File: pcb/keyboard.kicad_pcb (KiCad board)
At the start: 2 copper layers, 219 x 100.2 mm, 50 parts, among them J1 TRRS, SW11 11, SW12 12, SW13 13, SW14 14, SW15 15, SW16 16, SW17 17, SW18 18, SW19 19, SW21 21, SW22 22, SW23 23, SW24 24, SW25 25, SW26 26, SW27 27, SW28 28, SW29 29, SW31 31, SW32 32, SW33 33, SW34 34, SW35 35, SW36 36, SW37 37, SW38 38, SW39 39, SW41 41, SW42 42, SW43 43, SW45 45, SW46 46, SW47 47, SW48 48, SW49 49, U1 EliteC

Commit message: add traces to numpad
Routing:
- net (no net): track 385.5 -> 0.00 mm
- net COL9: track 0.00 -> 271.6 mm, vias 0 -> 4
- net COL8: track 0.00 -> 252.2 mm, vias 0 -> 4
- net COL7: track 0.00 -> 226.7 mm, vias 0 -> 4
- net ROW2: track 155.9 -> 276.8 mm
- net ROW4: track 40.3 -> 149.6 mm
- net ROW1: track 141.0 -> 235.3 mm
- net ROW3: track 174.9 -> 265.5 mm
- net Net-(SW27-Pad3): track 0.00 -> 33.5 mm
- net Net-(SW38-Pad3): track 0.00 -> 33.5 mm
- net Net-(SW48-Pad3): track 0.00 -> 33.5 mm
- net Net-(SW19-Pad3): track 0.00 -> 33.5 mm
- net Net-(SW49-Pad3): track 0.00 -> 33.5 mm
- net Net-(SW47-Pad3): track 0.00 -> 33.5 mm
- net Net-(SW29-Pad3): track 0.00 -> 33.5 mm
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
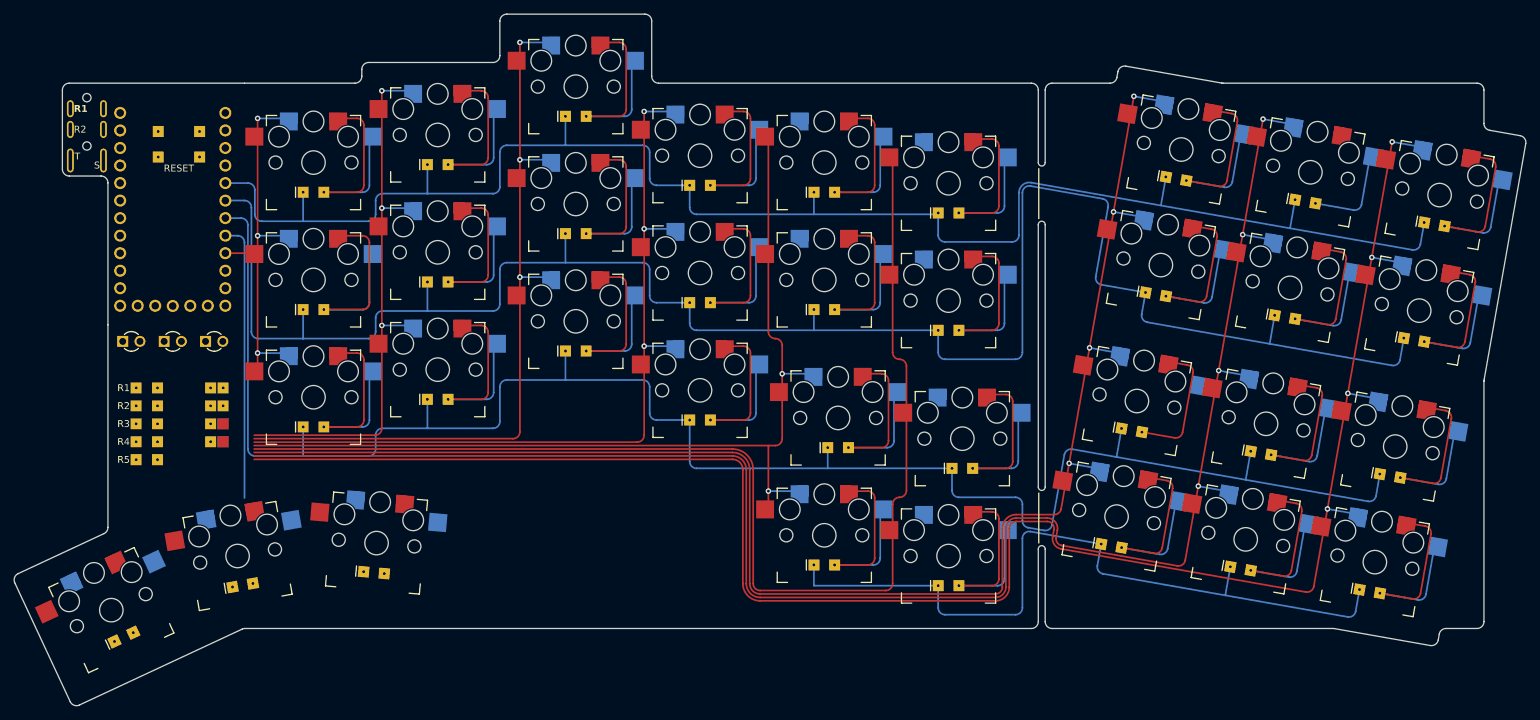
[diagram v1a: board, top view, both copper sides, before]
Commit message: use polygon instead of drill offset for switch footprint
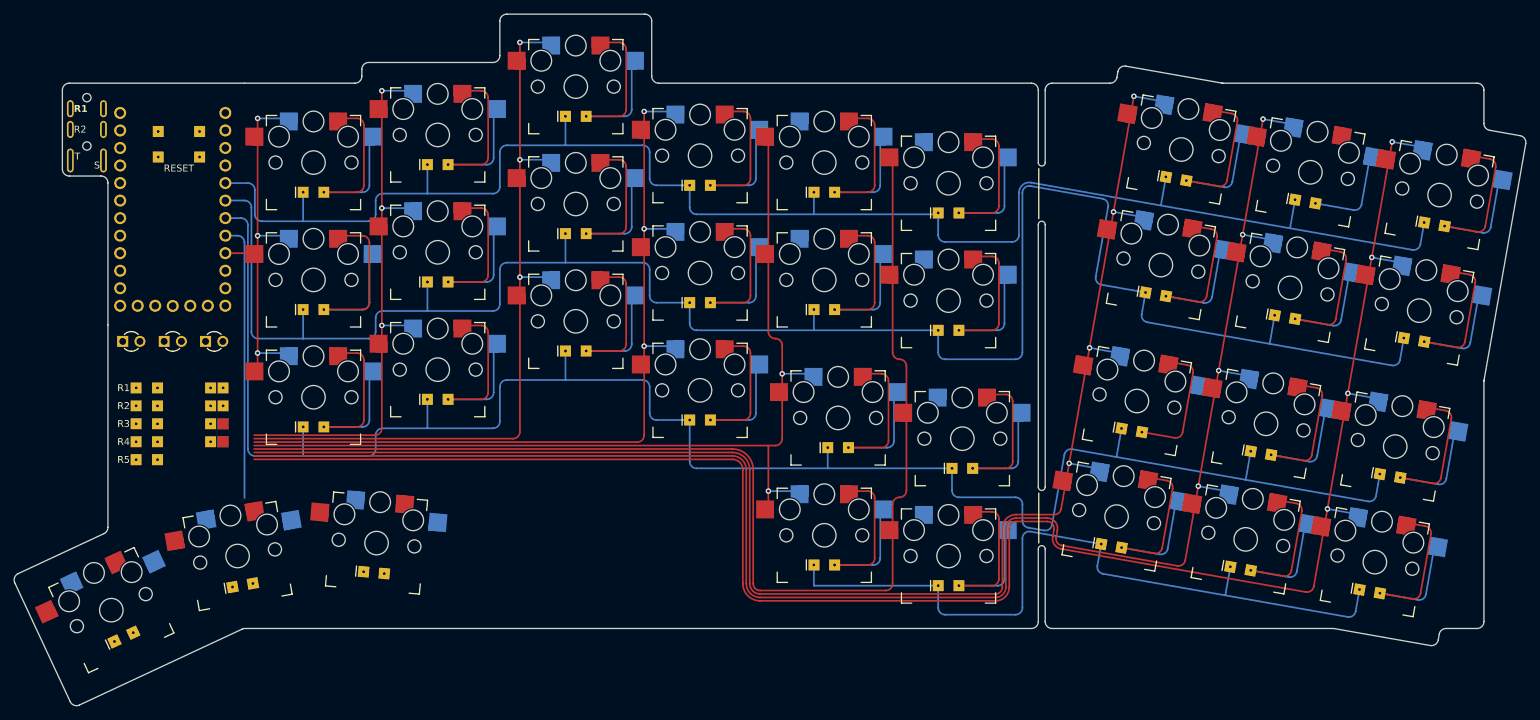
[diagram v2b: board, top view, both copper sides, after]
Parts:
- JP1, JP2: value Jumper -> JumperSplit

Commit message: correct traces with new layout
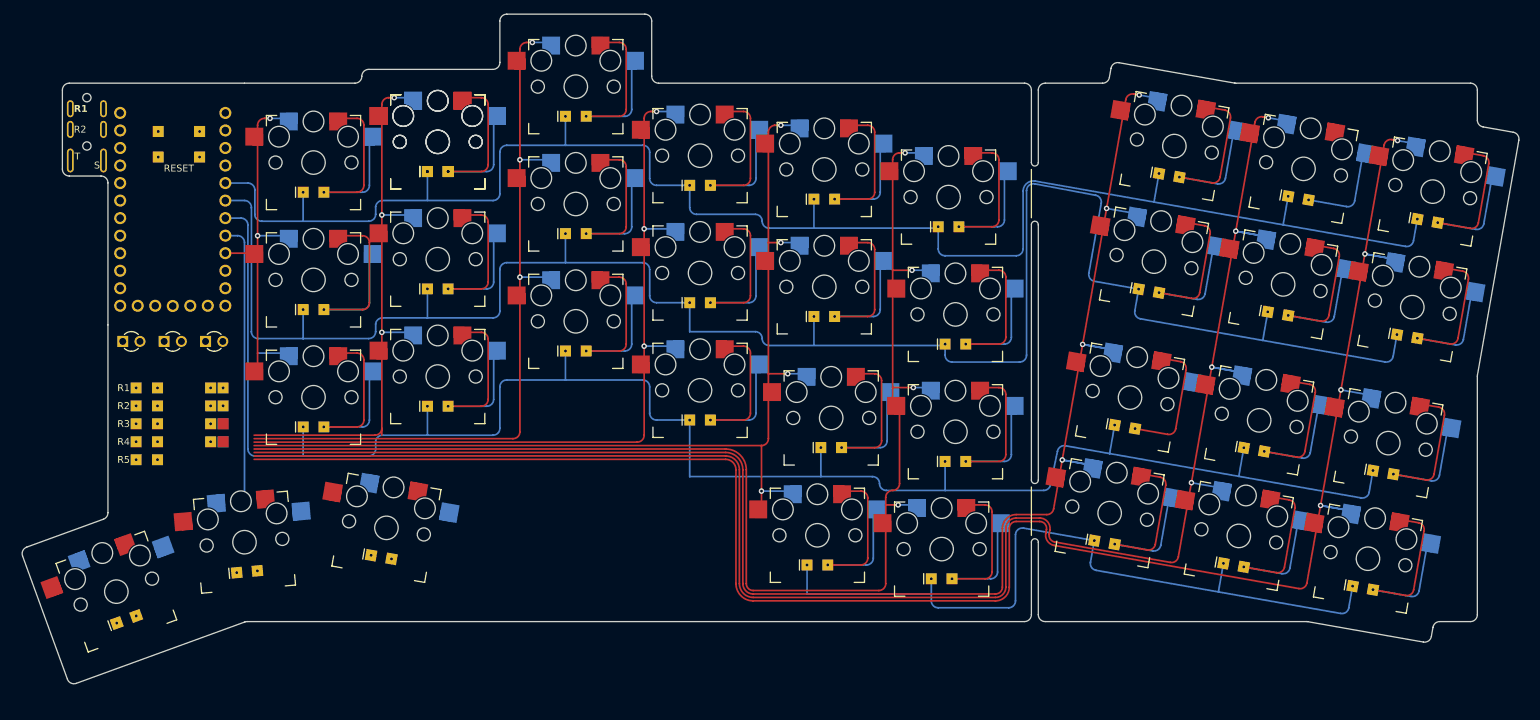
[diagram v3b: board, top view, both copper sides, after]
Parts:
- added SW12: 12, Keyboard:Switch, F.Cu at (99.5, 58.0)
- moved SW41 2.78 mm to (52.9, 123.2), turned to 20 degrees
- moved SW43 2.63 mm to (92.1, 113.9), turned to -10 degrees
- moved SW26 2.24 mm to (174.5, 83.0)
- moved SW42 2.24 mm to (71.5, 116.0), turned to 5 degrees
- moved SW16 2.00 mm to (173.5, 66.0)
- moved SW36 1.41 mm to (174.5, 100.0)
- moved SW46 1.41 mm to (172.5, 117.0)
- moved SW17 1.12 mm to (206.2, 58.6)
- moved SW18 1.12 mm to (224.9, 61.9)
- moved SW19 1.12 mm to (243.6, 65.2)
- moved SW27 1.12 mm to (203.3, 75.4)
- moved SW28 1.12 mm to (222.0, 78.7)
- moved SW29 1.12 mm to (240.7, 82.0)
- moved SW37 1.12 mm to (199.8, 95.0)
- moved SW38 1.12 mm to (218.5, 98.3)
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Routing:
- net COL6: track 175.1 -> 196.6 mm, vias 0 -> 4
- net COL5: track 141.1 -> 151.7 mm, vias 2 -> 4
- net COL7: track 226.7 -> 235.7 mm
- net COL8: track 252.2 -> 260.1 mm
- net COL9: track 271.6 -> 279.5 mm
- net ROW3: track 265.5 -> 260.8 mm
- net ROW1: track 235.3 -> 238.6 mm
- net ROW2: track 276.8 -> 278.0 mm
- net ROW4: track 149.6 -> 150.3 mm
- net COL1: track 56.8 -> 56.3 mm, vias 3 -> 2
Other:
- board size 219 x 100.2 mm -> 216.8 x 97 mm

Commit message: add traces for thumb cluster
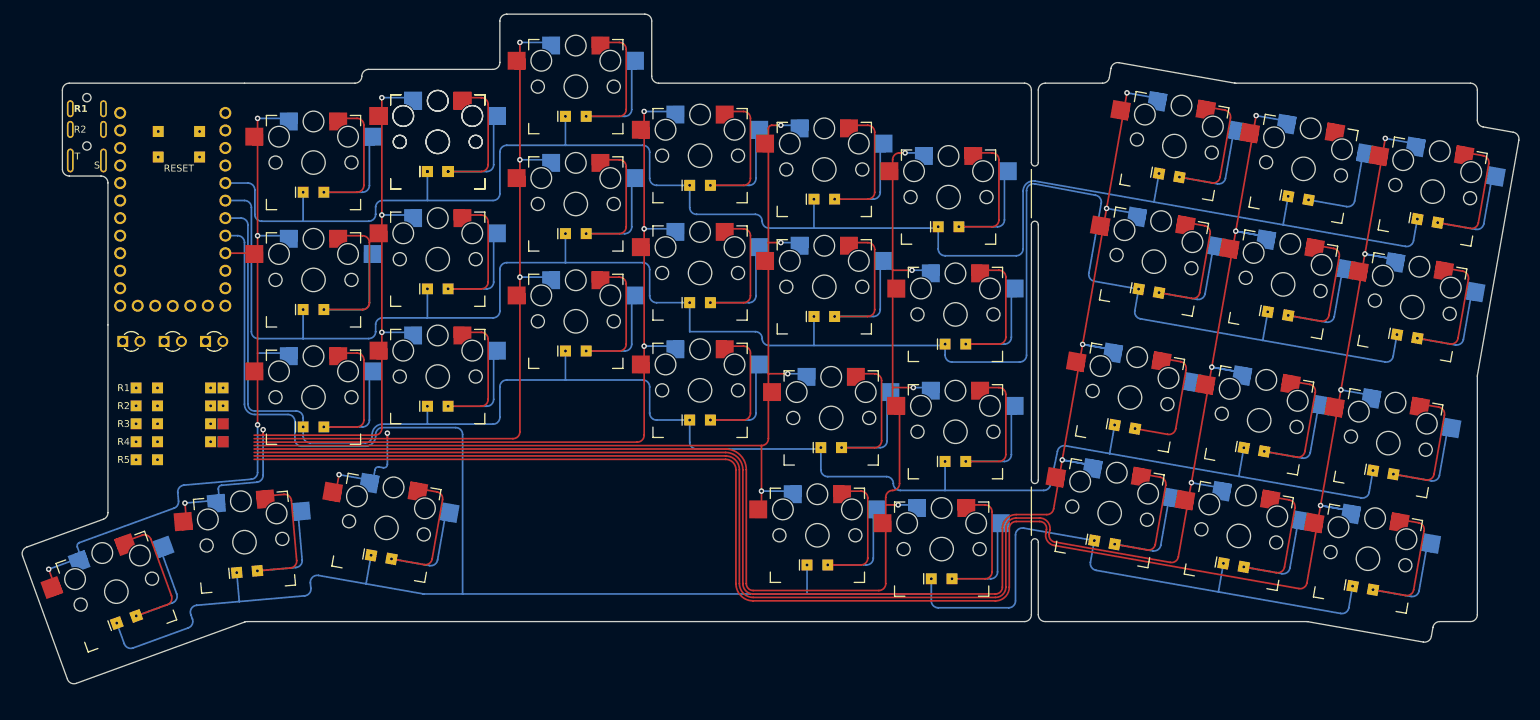
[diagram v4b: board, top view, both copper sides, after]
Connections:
- SW21 pad 3: Net-(SW21-Pad3) -> COL2
- SW21 pad 4: Net-(SW21-Pad3) -> COL2
- SW21 pad 5: Net-(SW21-Pad3) -> COL2
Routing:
- net ROW4: track 150.3 -> 314.3 mm
- net COL2: track 82.5 -> 141.5 mm, vias 3 -> 5
- net COL1: track 56.3 -> 111.3 mm, vias 2 -> 4
- net Net-(SW21-Pad3): track 35.1 -> 0.00 mm
- net Net-(SW42-Pad3): track 0.00 -> 33.5 mm
- net Net-(SW43-Pad3): track 0.00 -> 33.5 mm
- net Net-(SW41-Pad3): track 0.00 -> 33.5 mm
- net COL3: track 110.0 -> 127.7 mm, vias 3 -> 5
- net ROW3: track 260.8 -> 245.2 mm

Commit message: add remaining bad traces
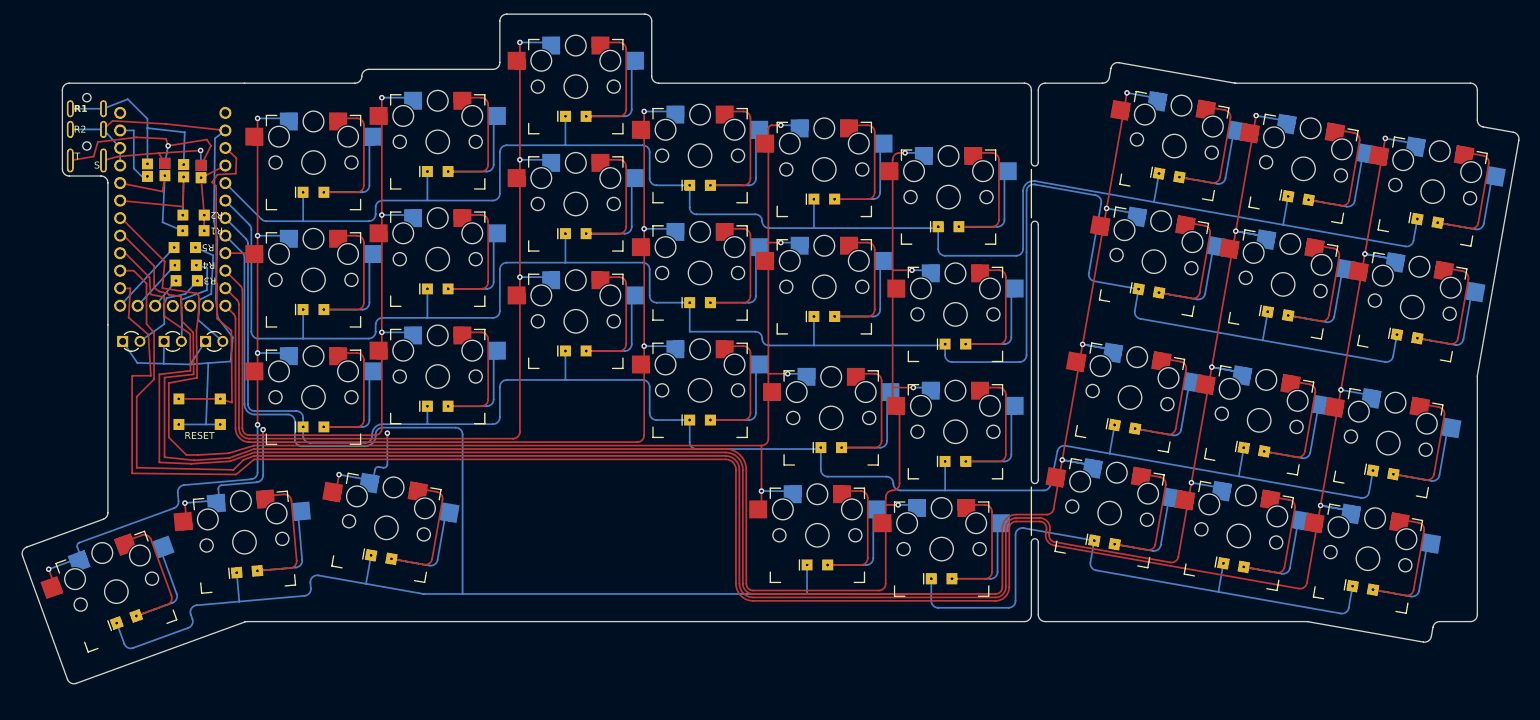
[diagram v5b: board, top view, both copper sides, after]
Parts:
- removed the SW12 at (99.5, 58.0)
- JP1, JP2: value JumperSplit -> Jumper
- moved JP4 40.2 mm to (60.0, 62.0), turned to 90 degrees
- moved SWRST1 38.9 mm to (65.0, 97.1)
- moved JP3 36.6 mm to (65.2, 62.3), turned to 90 degrees
- moved JP2 34.4 mm to (62.7, 62.2), turned to 90 degrees
- moved JP1 33.1 mm to (57.4, 62.1), turned to 90 degrees
- moved R5 31.2 mm to (62.9, 73.3), turned to 180 degrees
- moved R2 28.4 mm to (64.1, 68.6), turned to 180 degrees
- moved R4 26.2 mm to (63.0, 75.9), turned to 180 degrees
- moved R1 23.8 mm to (64.1, 70.9), turned to 180 degrees
- moved R3 21.5 mm to (63.1, 78.1), turned to 180 degrees
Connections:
- SW21 pad 3: COL2 -> Net-(SW21-Pad3)
- SW21 pad 4: COL2 -> Net-(SW21-Pad3)
- SW21 pad 5: COL2 -> Net-(SW21-Pad3)
- U1 pad 12: LED1 -> LED3
- U1 pad 26: LED3 -> LED1
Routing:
- net GND: track 0.00 -> 103.6 mm
- net COL5: track 151.9 -> 207.9 mm
- net COL6: track 196.6 -> 251.8 mm
- net COL7: track 236.1 -> 290.2 mm
- net COL9: track 280.0 -> 330.8 mm
- net COL8: track 260.6 -> 311.0 mm
- net RESET: track 0.00 -> 49.4 mm
- net Net-(SW21-Pad3): track 0.00 -> 33.5 mm
- net Net-(J1-Pad1): track 0.00 -> 29.2 mm
- net Net-(J1-Pad3): track 0.00 -> 29.1 mm, vias 0 -> 1
- net COL3: track 127.7 -> 151.8 mm
- net COL4: track 118.9 -> 141.0 mm
- net Net-(SW18-Pad3): track 13.7 -> 33.5 mm
- net SCL: track 0.00 -> 18.9 mm
- net SDA: track 0.00 -> 18.5 mm
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
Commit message: improve tracing around microcontroller
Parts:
- D1: renamed from LED1; value LED -> LED1
- D2: renamed from LED2; value LED -> LED2
- D3: renamed from LED3; value LED -> LED3
- moved SWRST1 4.28 mm to (61.1, 98.9)
- moved R2 3.36 mm to (60.9, 67.8)
- moved R1 3.30 mm to (60.9, 70.3)
- moved R3 2.28 mm to (60.9, 77.9)
- moved R4 2.18 mm to (60.9, 75.4)
- moved R5 2.05 mm to (60.9, 72.9)
- moved JP4 0.79 mm to (59.6, 62.7)
- moved JP2 0.76 mm to (62.1, 62.7)
- moved JP1 0.72 mm to (57.0, 62.7)
- moved JP3 0.67 mm to (64.7, 62.7)
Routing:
- net COL5: track 207.9 -> 216.6 mm
- net SCL: track 18.9 -> 11.6 mm
- net COL6: track 251.8 -> 257.7 mm
- net Net-(J1-Pad1): track 29.2 -> 34.4 mm
- net COL9: track 330.8 -> 326.2 mm
- net COL7: track 290.2 -> 294.3 mm
- net SDA: track 18.5 -> 15.0 mm
- net RESET: track 49.4 -> 51.9 mm
- net Net-(D2-A): track 14.8 -> 12.4 mm
- net COL8: track 311.0 -> 308.8 mm
- net Net-(D1-A): track 13.5 -> 11.4 mm
- net Net-(J1-Pad3): track 29.1 -> 27.3 mm
- net Net-(J1-Pad4): track 18.1 -> 16.4 mm
- net Net-(D3-A): track 17.9 -> 16.4 mm
- net DATA: track 9.93 -> 8.91 mm
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
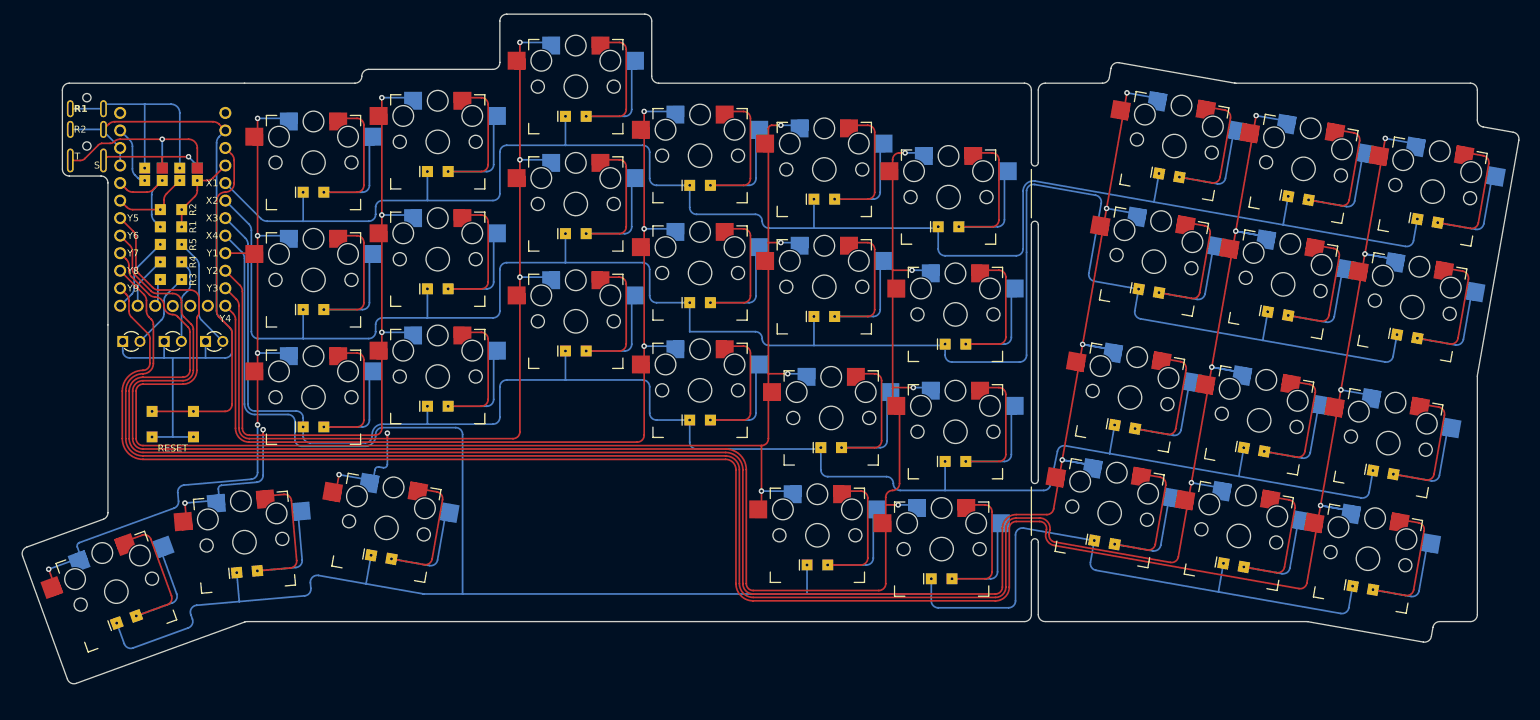
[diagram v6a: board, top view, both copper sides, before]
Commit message: fix silkscreen around microcontroller
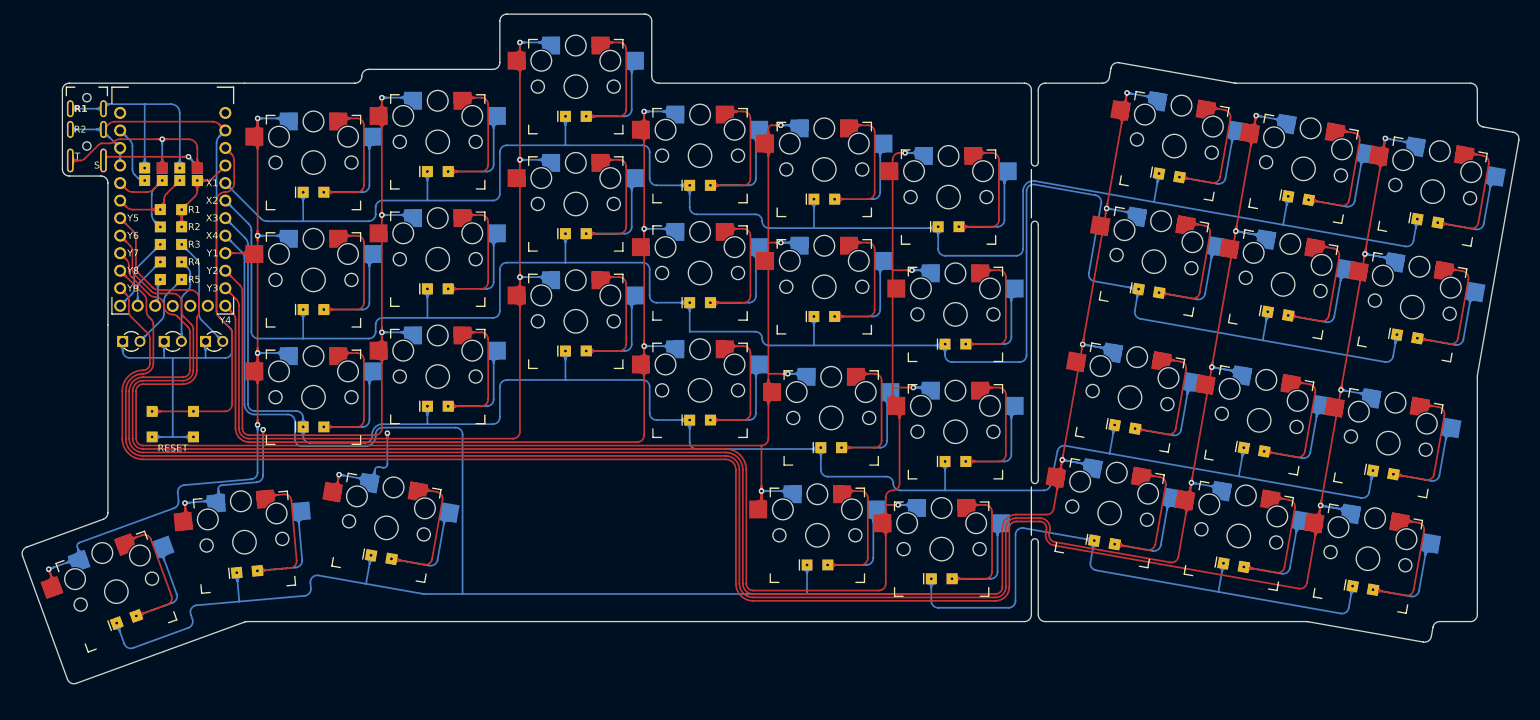
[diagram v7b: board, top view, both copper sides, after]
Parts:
- JP1: value Jumper -> J1
- JP2: value Jumper -> J2; footprint Keyboard:Jumper -> Keyboard:JumperSplit
- JP3: value JumperSplit -> J3; footprint Keyboard:JumperSplit -> Keyboard:Jumper
- JP4: value JumperSplit -> J4
- R1: renamed from R2; value R -> R1
- R2: renamed from R1; value R -> R2
- R3: renamed from R5; value R -> R3
- R4: value R -> R4
- R5: renamed from R3; value R -> R5
- moved JP4 5.08 mm to (64.7, 62.7)
- moved JP2 2.54 mm to (59.6, 62.7)
- moved JP3 2.54 mm to (62.1, 62.7)
- turned R1 to 0 degrees
- turned R2 to 0 degrees
- turned R3 to 0 degrees
- turned R4 to 0 degrees
- turned R5 to 0 degrees
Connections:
- JP2 pad 1: SCL -> SDA
- JP2 pad 2: Net-(J1-Pad1) -> Net-(J1-Pad4)
- JP3 pad 1: VCC -> SCL
- JP3 pad 2: Net-(J1-Pad3) -> Net-(J1-Pad1)
- JP4 pad 1: SDA -> VCC
- JP4 pad 2: Net-(J1-Pad4) -> Net-(J1-Pad3)
- JP4 pad 3: Net-(J1-Pad3) -> Net-(J1-Pad4)
- R1 pad 1: VCC -> SCL
- R1 pad 2: SCL -> VCC
- R2 pad 1: VCC -> SDA
- R2 pad 2: SDA -> VCC
- R3 pad 1: Net-(D3-A) -> LED3
- R3 pad 2: LED3 -> Net-(D3-A)
- R4 pad 1: Net-(D2-A) -> LED2
- R4 pad 2: LED2 -> Net-(D2-A)
- R5 pad 1: Net-(D1-A) -> LED1
- R5 pad 2: LED1 -> Net-(D1-A)
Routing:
- net COL1: track 111.3 -> 148.8 mm
- net COL8: track 308.8 -> 344.6 mm
- net COL9: track 326.2 -> 362.0 mm
- net COL7: track 294.3 -> 330.1 mm
- net COL2: track 132.4 -> 168.0 mm
- net COL3: track 151.7 -> 187.2 mm
- net COL5: track 216.6 -> 246.6 mm
- net COL6: track 257.7 -> 284.5 mm
- net COL4: track 141.0 -> 165.8 mm
- net ROW2: track 276.0 -> 300.2 mm
- net ROW3: track 243.6 -> 267.8 mm
- net ROW1: track 236.2 -> 258.5 mm
- net GND: track 103.3 -> 125.4 mm
- net ROW4: track 313.1 -> 331.7 mm
- net VCC: track 12.5 -> 22.5 mm
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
